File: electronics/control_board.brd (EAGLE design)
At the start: 190 x 180 mm, 137 parts, among them J17 JST_PH_B3B-PH-K-S(LF)(SN), J18 JST_PH_B3B-PH-K-S(LF)(SN), J19 JST_PH_B3B-PH-K-S(LF)(SN), J20 JST_PH_B3B-PH-K-S(LF)(SN), J21 JST_PH_B3B-PH-K-S(LF)(SN), J22 JST_PH_B3B-PH-K-S(LF)(SN), J23 JST_PH_B3B-PH-K-S(LF)(SN), J24 JST_PH_B3B-PH-K-S(LF)(SN), J25 JST_PH_B3B-PH-K-S(LF)(SN), J26 JST_PH_B3B-PH-K-S(LF)(SN), J27 JST_PH_B3B-PH-K-S(LF)(SN), J28 JST_PH_B3B-PH-K-S(LF)(SN), J29 JST_PH_B3B-PH-K-S(LF)(SN), J30 JST_PH_B3B-PH-K-S(LF)(SN), J31 JST_PH_B3B-PH-K-S(LF)(SN), J32 JST_PH_B3B-PH-K-S(LF)(SN), U18 AD7730BRUZ, U19 AD5360BSTZ, U20 ADR425ARZ, U21 AD7730BRUZ, U23 AD7730BRUZ, U24 AD7730BRUZ, U25 AD7730BRUZ, U26 AD7730BRUZ, U27 AD7730BRUZ, U28 AD7730BRUZ, U4 ADR421ARZ, U5 AD7616BSTZ, X1 22-23-2031, Y1 KC2520B-C1, Y3 KC2520B-C1

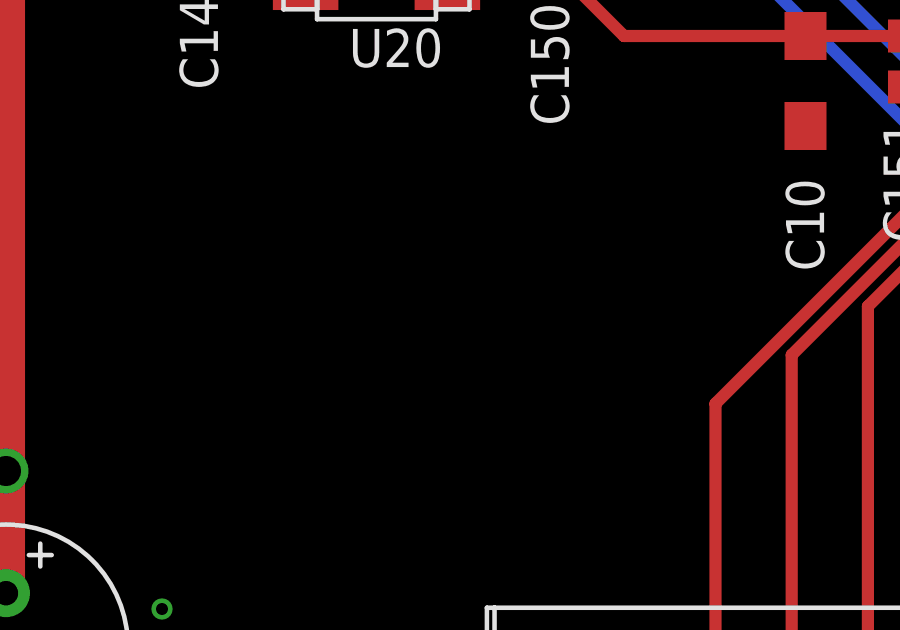
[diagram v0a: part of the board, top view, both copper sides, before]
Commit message: added firmware code snippets
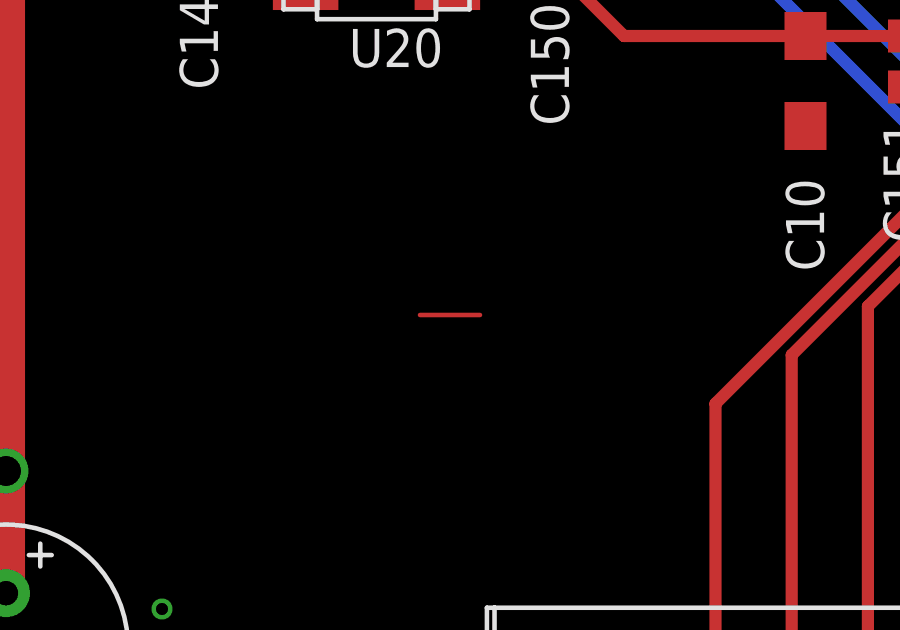
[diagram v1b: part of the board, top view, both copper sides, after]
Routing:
- net N$1: track 0.00 -> 2.00 mm
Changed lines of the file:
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@@
 <drawing>
 <settings>
-<setting alwaysvectorfont="yes"/>
+<setting alwaysvectorfont="no"/>
 <setting verticaltext="up"/>
 </settings>
@@
 <wire x1="4.072" y1="146.9" x2="0.45" y2="146.9" width="1.016" layer="1"/>
 </signal>
+<signal name="N$1">
+<wire x1="110" y1="38.35" x2="112" y2="38.35" width="0.1524" layer="1"/>
+</signal>
 </signals>

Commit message: teensy test v0.0
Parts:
- R1, R3: value 68 -> 120
- R10: value 680 -> 1k
- R11: value 330 -> 120
- R5: value 220 -> 330
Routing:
- net N$1: track 2.00 -> 0.00 mm
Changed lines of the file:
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@@
 <attribute name="VALUE" x="7.305" y="172.272" size="1.27" layer="51" align="center"/>
 </element>
-<element name="R1" library="resistor" library_urn="urn:adsk.eagle:library:348" package="R0805" package3d_urn="urn:adsk.eagle:package:26059/1" value="68" x="160.55" y="166.4" smashed="yes" rot="R270">
+<element name="R1" library="resistor" library_urn="urn:adsk.eagle:library:348" package="R0805" package3d_urn="urn:adsk.eagle:package:26059/1" value="120" x="160.55" y="166.4" smashed="yes" rot="R270">
 <attribute name="NAME" x="159.87" y="164.135" size="1.27" layer="25" rot="R270"/>
 <attribute name="VALUE" x="158.01" y="167.035" size="1.27" layer="27" rot="R270"/>
 </element>
-<element name="R3" library="resistor" library_urn="urn:adsk.eagle:library:348" package="R0805" package3d_urn="urn:adsk.eagle:package:26059/1" value="68" x="154.7" y="166.4" smashed="yes" rot="R270">
+<element name="R3" library="resistor" library_urn="urn:adsk.eagle:library:348" package="R0805" package3d_urn="urn:adsk.eagle:package:26059/1" value="120" x="154.7" y="166.4" smashed="yes" rot="R270">
 <attribute name="NAME" x="154.02" y="164.085" size="1.27" layer="25" rot="R270"/>
 <attribute name="VALUE" x="152.16" y="167.035" size="1.27" layer="27" rot="R270"/>
 </element>
-<element name="R5" library="resistor" library_urn="urn:adsk.eagle:library:348" package="R0805" package3d_urn="urn:adsk.eagle:package:26059/1" value="220" x="148.85" y="166.4" smashed="yes" rot="R270">
+<element name="R5" library="resistor" library_urn="urn:adsk.eagle:library:348" package="R0805" package3d_urn="urn:adsk.eagle:package:26059/1" value="330" x="148.85" y="166.4" smashed="yes" rot="R270">
 <attribute name="NAME" x="148.17" y="164.135" size="1.27" layer="25" rot="R270"/>
 <attribute name="VALUE" x="146.31" y="167.035" size="1.27" layer="27" rot="R270"/>
 </element>
-<element name="R10" library="resistor" library_urn="urn:adsk.eagle:library:348" package="R0805" package3d_urn="urn:adsk.eagle:package:26059/1" value="680" x="166.4" y="166.4" smashed="yes" rot="R270">
+<element name="R10" library="resistor" library_urn="urn:adsk.eagle:library:348" package="R0805" package3d_urn="urn:adsk.eagle:package:26059/1" value="1k" x="166.4" y="166.4" smashed="yes" rot="R270">
 <attribute name="NAME" x="165.77" y="164.135" size="1.27" layer="25" rot="R270"/>
 <attribute name="VALUE" x="163.86" y="167.035" size="1.27" layer="27" rot="R270"/>
@@
 <attribute name="VALUE" x="-8.33" y="157.21" size="1.27" layer="27" ratio="10" rot="R270"/>
 </element>
-<element name="R11" library="resistor" library_urn="urn:adsk.eagle:library:348" package="R0805" package3d_urn="urn:adsk.eagle:package:26059/1" value="330" x="17.6" y="141.05" smashed="yes">
+<element name="R11" library="resistor" library_urn="urn:adsk.eagle:library:348" package="R0805" package3d_urn="urn:adsk.eagle:package:26059/1" value="120" x="17.6" y="141.05" smashed="yes">
 <attribute name="NAME" x="16.315" y="142.32" size="1.27" layer="25"/>
 <attribute name="VALUE" x="16.965" y="138.51" size="1.27" layer="27"/>
@@
 <wire x1="4.072" y1="146.9" x2="0.45" y2="146.9" width="1.016" layer="1"/>
 </signal>
-<signal name="N$1">
-<wire x1="110" y1="38.35" x2="112" y2="38.35" width="0.1524" layer="1"/>
-</signal>
 </signals>
